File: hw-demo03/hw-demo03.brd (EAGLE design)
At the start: 83.5 x 63.5 mm, 42 parts, among them IC3 MCP2562T, IC4 STM32F042

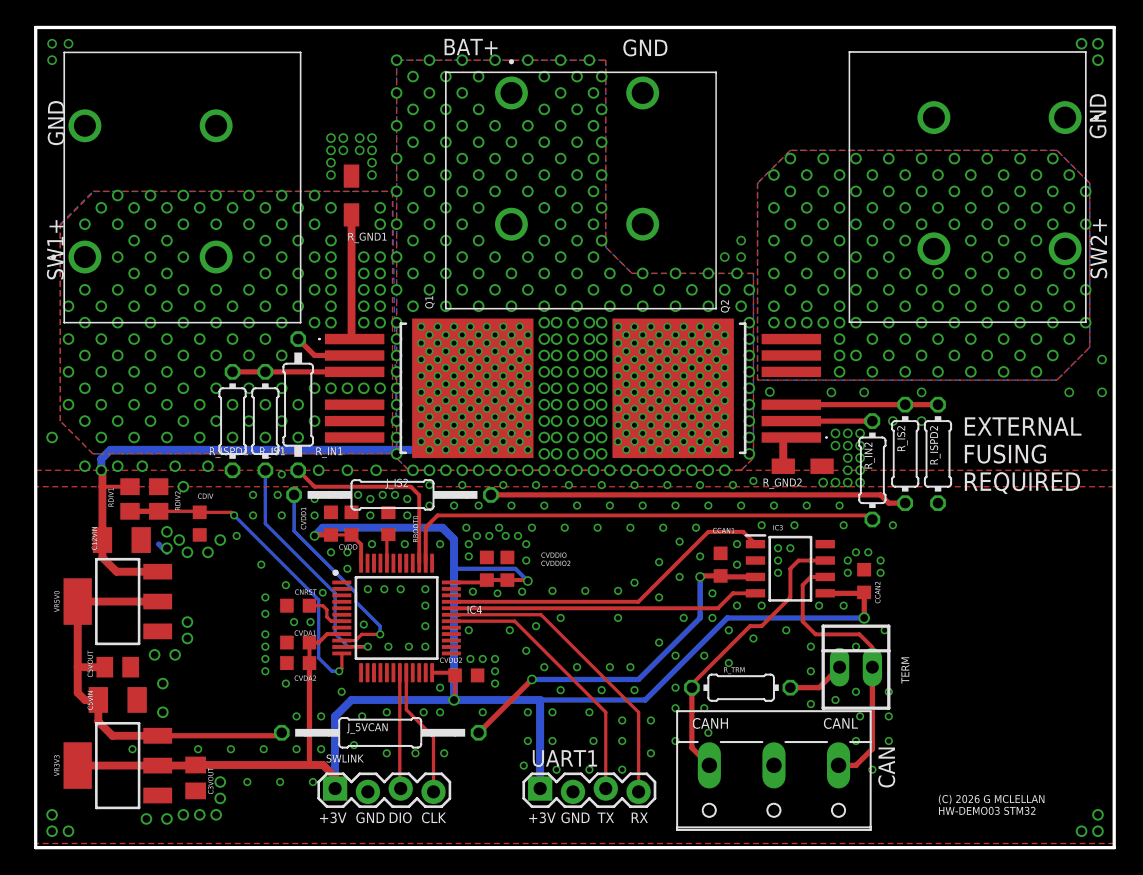
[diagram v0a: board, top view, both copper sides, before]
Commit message: footprint too big, will try something else
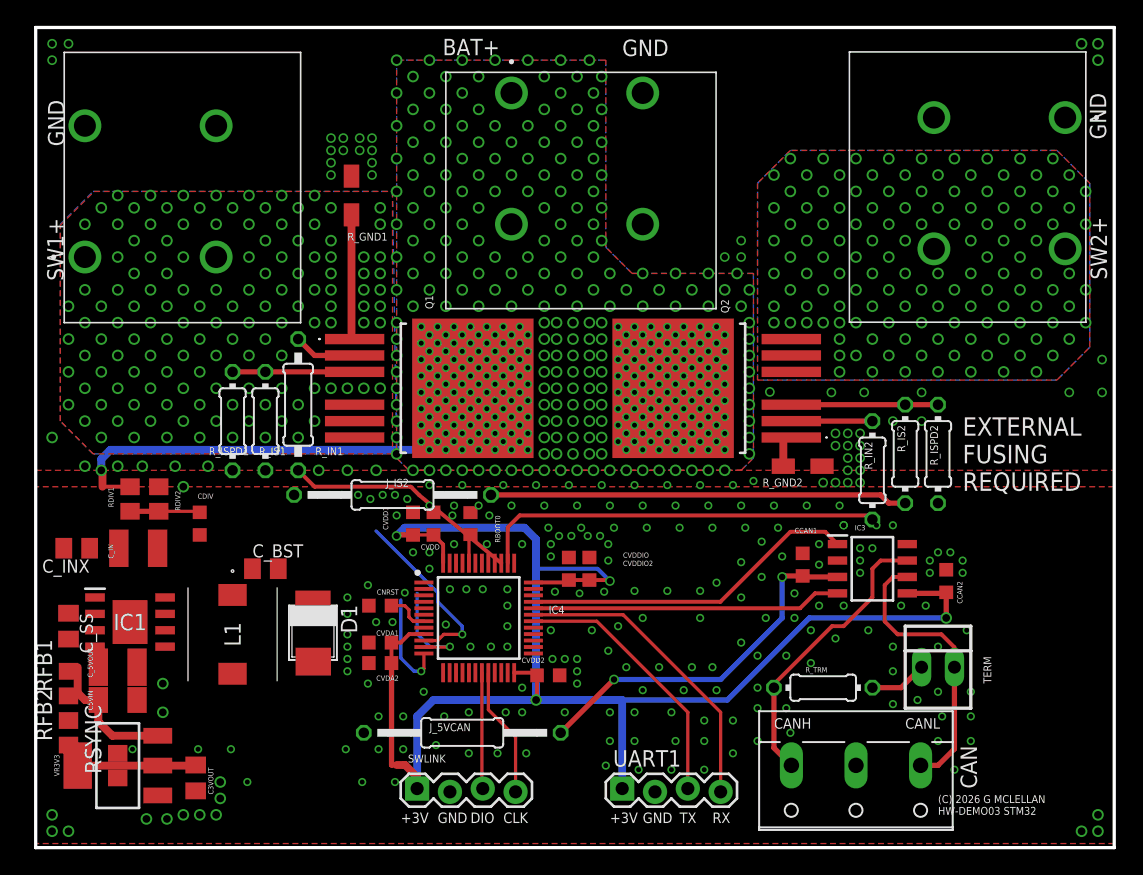
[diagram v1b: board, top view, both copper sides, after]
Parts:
- removed C12VIN: 1u, rcl:C1206K
- removed C5VOUT: 1u, rcl:C0805K
- removed VR5V0: (no value), SparkFun-PowerIC:SOT223
- added C_5VOUT: 47u, rcl:C1210K
- added C_BST: 10n, rcl:C0805K
- added C_IN: 10u, rcl:C1210K
- added C_INX: 1u, rcl:C0805K
- added C_SS: 100n, rcl:C0805K
- added D1: (no value), diode-special-packages:SMB
- added IC1: LM22680QMRE, LM22680QMRE-ADJ_NOPB:SOIC127P600X170-9N
- added L1: 15uH, CLF7045NIT-150M-D:CLF7045_*
- added RFB1: 1K0, rcl:R0805
- added RFB2: 2K87, rcl:R0805
- added RSYNC: 75K, rcl:R0805
- moved IC3 6.35 mm to (66.0, 21.6)
- moved TERM 6.35 mm to (71.1, 14.0)
- moved CCAN1 6.35 mm to (60.6, 21.9)
- moved CNRST 6.35 mm to (27.9, 18.7)
- moved CVDA1 6.35 mm to (27.9, 15.9)
- moved CVDA2 6.35 mm to (27.9, 14.3)
- moved CVDD 6.35 mm to (32.1, 25.1)
- moved CVDD1 6.35 mm to (30.5, 25.1)
- moved CVDD2 6.35 mm to (41.0, 13.3)
- moved CVDDIO 6.35 mm to (44.1, 21.6)
- moved CVDDIO2 6.35 mm to (42.5, 21.6)
- moved IC4 6.35 mm to (35.6, 17.8)
- moved UART1 6.35 mm to (46.7, 4.45)
- moved J_5VCAN 6.35 mm to (34.3, 8.89)
- moved RBOOT0 6.35 mm to (34.9, 25.1)
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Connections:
- new net BOOST: C_BST.1, IC1.1
- new net FB: IC1.4, RFB1.1, RFB2.2
- new net SS: C_SS.1, IC1.2
- new net SW: C_BST.2, D1.K, IC1.8, L1.1
- new net SYNC: IC1.3, RSYNC.2
- net +12V: now also C_IN.1, C_INX.1, IC1.7; no longer C12VIN.1, VR5V0.3
- net +5V: now also C_5VOUT.1, L1.2, RFB1.2; no longer C5VOUT.1, VR5V0.2, VR5V0.4
- net GND: now also C_5VOUT.2, C_IN.2, C_INX.2, C_SS.2, D1.A, IC1.6, RFB2.1, RSYNC.1; no longer C12VIN.2, C5VOUT.2, VR5V0.1
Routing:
- net +5V: track 33.9 -> 10.9 mm
- net ADC2: track 25.5 -> 13.4 mm, vias 2 -> 1
- net ADC1: track 19.9 -> 8.12 mm
- net +12V: track 40.3 -> 30.1 mm
- net +3V3: track 141.3 -> 132.1 mm
- net CTL2: track 37.9 -> 31.5 mm
- net CTL1: track 15.4 -> 18.4 mm
- net ADC3: track 16.7 -> 13.9 mm
- net GND: track 0.90 -> 0.00 mm, vias 279 -> 261
